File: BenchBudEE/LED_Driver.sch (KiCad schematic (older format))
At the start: 0 parts

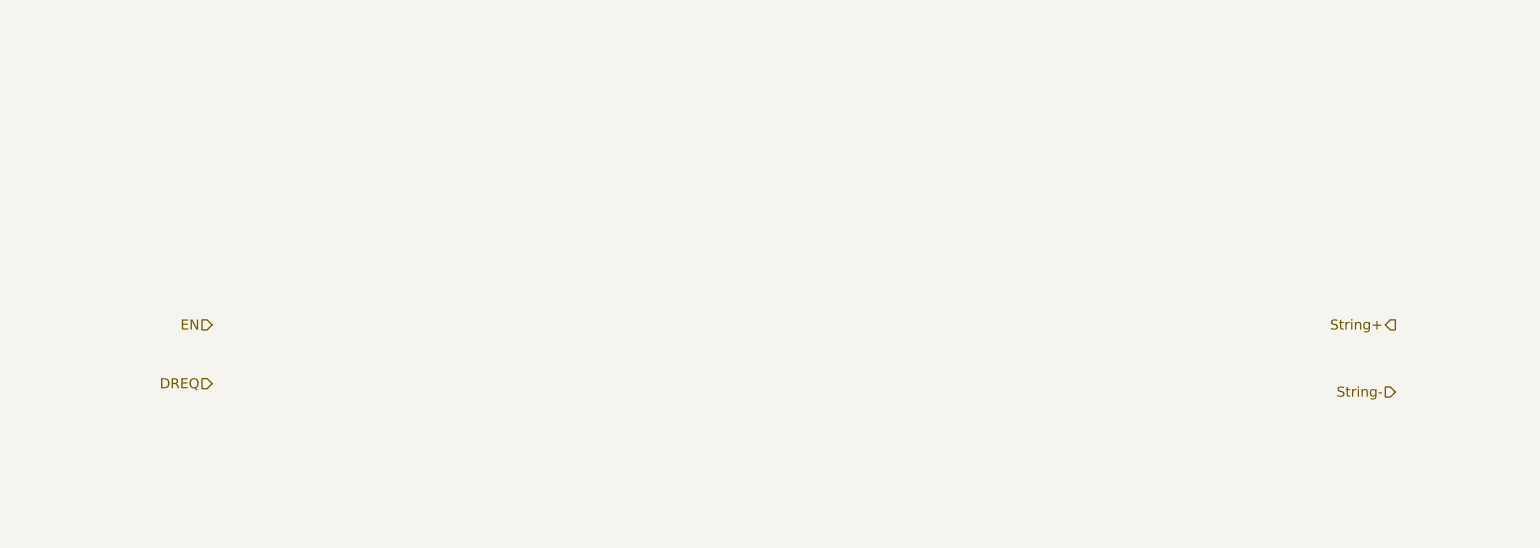
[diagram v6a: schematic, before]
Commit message: Populated the LED Driver block based on the AP5726.
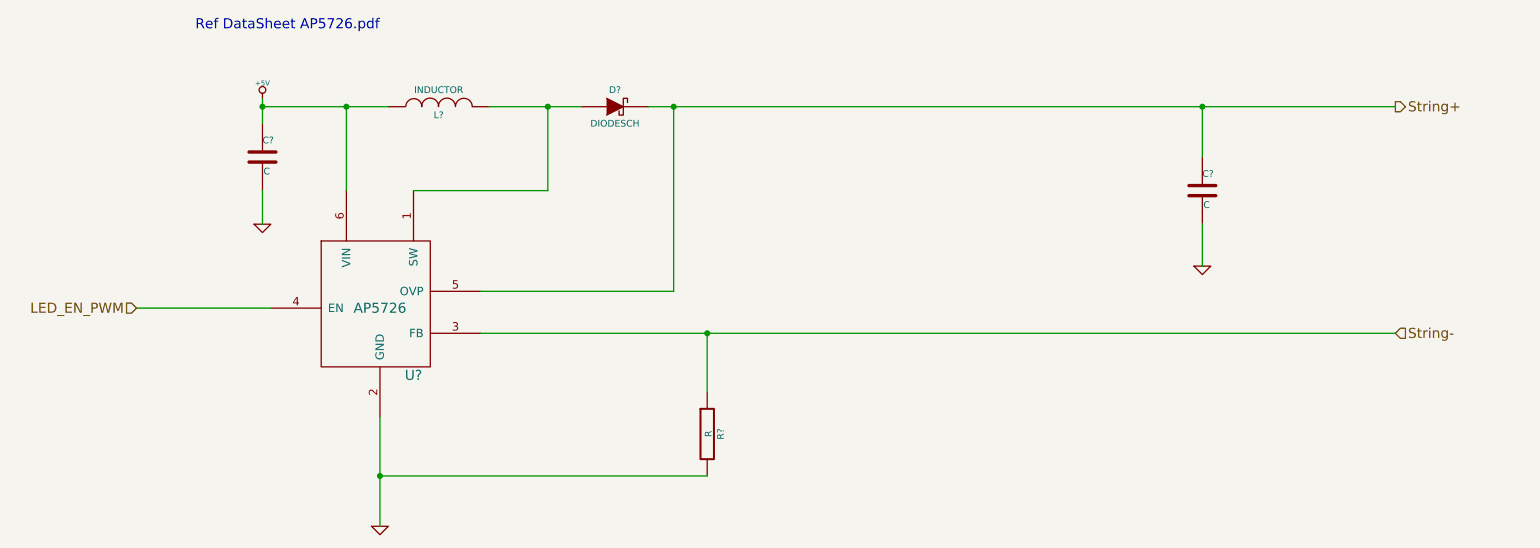
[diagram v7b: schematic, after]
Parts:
- added C? (x2): C, ~, symbol C
- added D?: DIODESCH, ~, symbol DIODESCH
- added L?: INDUCTOR, ~, symbol INDUCTOR
- added R?: R, ~, symbol R
- added U?: AP5726, symbol AP5726
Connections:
- net String+: now also C?.1, D?.2 (K), U?.5 (OVP)
- net String-: now also R?.1, U?.3 (FB)
- new net: D?.1 (A), L?.2, U?.1 (SW)
- new net +5V: C?.1, L?.1, U?.6 (VIN)
- new net GND: C?.2, C?.2, R?.2, U?.2 (GND)
- new net LED_EN_PWM: U?.4 (EN)
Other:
- note added: "Ref DataSheet AP5726.pdf"
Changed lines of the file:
@@
 Sheet 6 9
 Title ""
-Date "9 feb 2014"
+Date "10 feb 2014"
 Rev ""
 Comp ""
@@
 Comment4 ""
 $EndDescr
-Text HLabel 2050 2400 0    60   Input ~ 0
-EN
-Text HLabel 2050 2750 0    60   Input ~ 0
-DREQ
-Text HLabel 9100 2400 0    60   Output ~ 0
+Text HLabel 1600 2300 0    60   Input ~ 0
+LED_EN_PWM
+Text HLabel 9100 1100 2    60   Output ~ 0
 String+
-Text HLabel 9100 2800 0    60   Input ~ 0
+Text HLabel 9100 2450 2    60   Input ~ 0
 String-
+$Comp
+L AP5726 U?
+U 1 1 52F83C82
+P 3050 2300
+F 0 "U?" H 3250 1900 60  0000 C CNN
+F 1 "AP5726" H 3050 2300 60  0000 C CNN
+F 2 "" H 3050 2300 60  0000 C CNN
+F 3 "" H 3050 2300 60  0000 C CNN
+	1    3050 2300
+	1    0    0    -1
+$EndComp
+Wire Wire Line
+	1600 2300 2400 2300
+$Comp
+L +5V #PWR?
+U 1 1 52F8436F
+P 2350 1050
+F 0 "#PWR?" H 2350 1140 20  0001 C CNN
+F 1 "+5V" H 2350 1140 30  0000 C CNN
+F 2 "" H 2350 1050 60  0000 C CNN
+F 3 "" H 2350 1050 60  0000 C CNN
+	1    2350 1050
+	1    0    0    -1
+$EndComp
+$Comp
+L GND #PWR?
+U 1 1 52F8437E
+P 2350 1800
+F 0 "#PWR?" H 2350 1800 30  0001 C CNN
+F 1 "GND" H 2350 1730 30  0001 C CNN
+F 2 "" H 2350 1800 60  0000 C CNN
+F 3 "" H 2350 1800 60  0000 C CNN
+	1    2350 1800
+	1    0    0    -1
+$EndComp
+$Comp
+L GND #PWR?
+U 1 1 52F8438B
+P 3050 3600
+F 0 "#PWR?" H 3050 3600 30  0001 C CNN
+F 1 "GND" H 3050 3530 30  0001 C CNN
+F 2 "" H 3050 3600 60  0000 C CNN
+F 3 "" H 3050 3600 60  0000 C CNN
+	1    3050 3600
+	1    0    0    -1
+$EndComp
+Wire Wire Line
+	3050 2950 3050 3600
+$Comp
+L C C?
+U 1 1 52F84395
+P 2350 1400
+F 0 "C?" H 2350 1500 40  0000 L CNN
+F 1 "C" H 2356 1315 40  0000 L CNN
+F 2 "~" H 2388 1250 30  0000 C CNN
+F 3 "~" H 2350 1400 60  0000 C CNN
+	1    2350 1400
+	1    0    0    -1
+$EndComp
+Wire Wire Line
+	2350 1600 2350 1800
+Wire Wire Line
+	2350 1050 2350 1200
+Wire Wire Line
+	2350 1100 3100 1100
+Wire Wire Line
+	2850 1100 2850 1600
+Connection ~ 2350 1100
+$Comp
+L C C?
+U 1 1 52F845D8
+P 7950 1600
+F 0 "C?" H 7950 1700 40  0000 L CNN
+F 1 "C" H 7956 1515 40  0000 L CNN
+F 2 "~" H 7988 1450 30  0000 C CNN
+F 3 "~" H 7950 1600 60  0000 C CNN
+	1    7950 1600
+	1    0    0    -1
+$EndComp
+$Comp
+L INDUCTOR L?
+U 1 1 52F845E0
+P 3400 1100
+F 0 "L?" V 3350 1100 40  0000 C CNN
+F 1 "INDUCTOR" V 3500 1100 40  0000 C CNN
+F 2 "~" H 3400 1100 60  0000 C CNN
+F 3 "~" H 3400 1100 60  0000 C CNN
+	1    3400 1100
+	0    -1   -1   0
+$EndComp
+Connection ~ 2850 1100
+Wire Wire Line
+	3700 1100 4250 1100
+Wire Wire Line
+	4050 1100 4050 1600
+Wire Wire Line
+	4050 1600 3250 1600
+$Comp
+L DIODESCH D?
+U 1 1 52F84602
+P 4450 1100
+F 0 "D?" H 4450 1200 40  0000 C CNN
+F 1 "DIODESCH" H 4450 1000 40  0000 C CNN
+F 2 "~" H 4450 1100 60  0000 C CNN
+F 3 "~" H 4450 1100 60  0000 C CNN
+	1    4450 1100
+	1    0    0    -1
+$EndComp
+Connection ~ 4050 1100
+Wire Wire Line
+	4650 1100 9100 1100
+Wire Wire Line
+	7950 1100 7950 1400
+Text Notes 1950 650  0    60   ~ 0
+Ref DataSheet AP5726.pdf
+$Comp
+L GND #PWR?
+U 1 1 52F84869
+P 7950 2050
+F 0 "#PWR?" H 7950 2050 30  0001 C CNN
+F 1 "GND" H 7950 1980 30  0001 C CNN
+F 2 "" H 7950 2050 60  0000 C CNN
+F 3 "" H 7950 2050 60  0000 C CNN
+	1    7950 2050
+	1    0    0    -1
+$EndComp
+Wire Wire Line
+	7950 2050 7950 1800
+Connection ~ 7950 1100
+$Comp
+L R R?
+U 1 1 52F84AC1
+P 5000 3050
+F 0 "R?" V 5080 3050 40  0000 C CNN
+F 1 "R" V 5007 3051 40  0000 C CNN
+F 2 "~" V 4930 3050 30  0000 C CNN
+F 3 "~" H 5000 3050 30  0000 C CNN
+	1    5000 3050
+	1    0    0    -1
+$EndComp
+Wire Wire Line
+	5000 3300 3050 3300
+Connection ~ 3050 3300
+Wire Wire Line
+	5000 2800 5000 2450
+Wire Wire Line
+	3650 2450 9100 2450
+Wire Wire Line
+	3650 2200 4800 2200
+Wire Wire Line
+	4800 2200 4800 1100
+Connection ~ 4800 1100
+Connection ~ 5000 2450
 $EndSCHEMATC

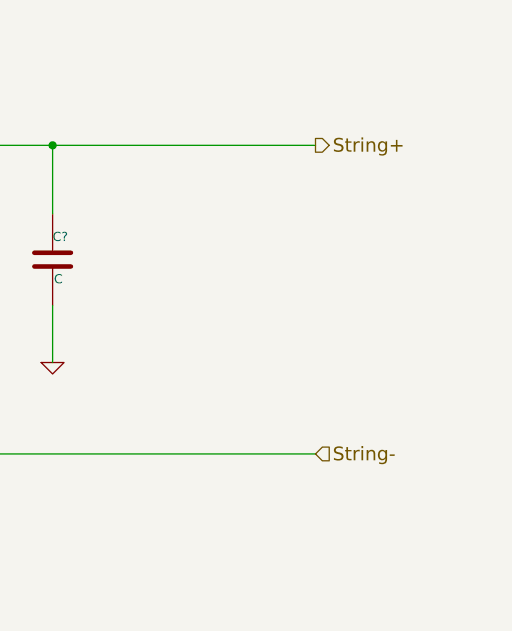
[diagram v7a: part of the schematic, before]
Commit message: Populated the Arduino block and top level wiring.
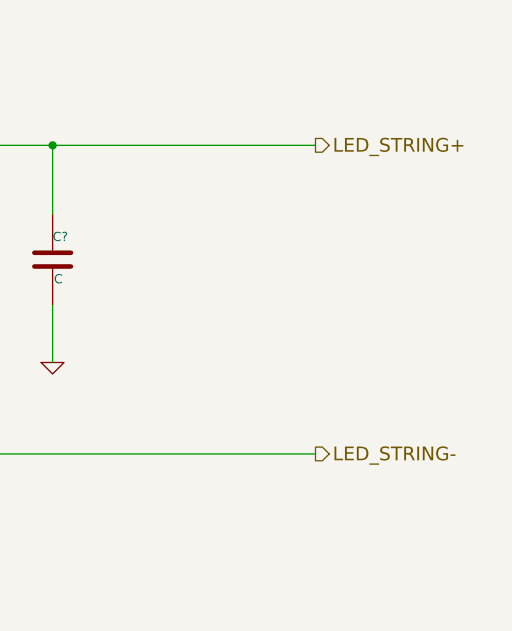
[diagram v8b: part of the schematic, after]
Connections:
- net String+ renamed LED_STRING+
- net String- renamed LED_STRING-
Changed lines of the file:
@@
 LED_EN_PWM
 Text HLabel 9100 1100 2    60   Output ~ 0
-String+
-Text HLabel 9100 2450 2    60   Input ~ 0
-String-
+LED_STRING+
+Text HLabel 9100 2450 2    60   Output ~ 0
+LED_STRING-
 $Comp
 L AP5726 U?
